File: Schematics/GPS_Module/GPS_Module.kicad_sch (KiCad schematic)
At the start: 70 parts, among them J1 GT8E-6P-2H(55), J2 SWD_01x04_Pin, J4 Stack Male Edge Connector, J4 USB_C_Female_USB2_Small, Q1 AO3400A, SW1 SW_STM_RESET, SW2 SW_STM_BOOT_MODE, U1 STM32F103CBT6, U12 AMS1117-3.3, U2 W25Q128JVS, U4 LM66100DCKR, U5 LM66100DCKR, U6 LM66100DCKR, U8 ACS70331EOLC, U9 ISO1042BQDWVR, Y1 X322516MMB4SI

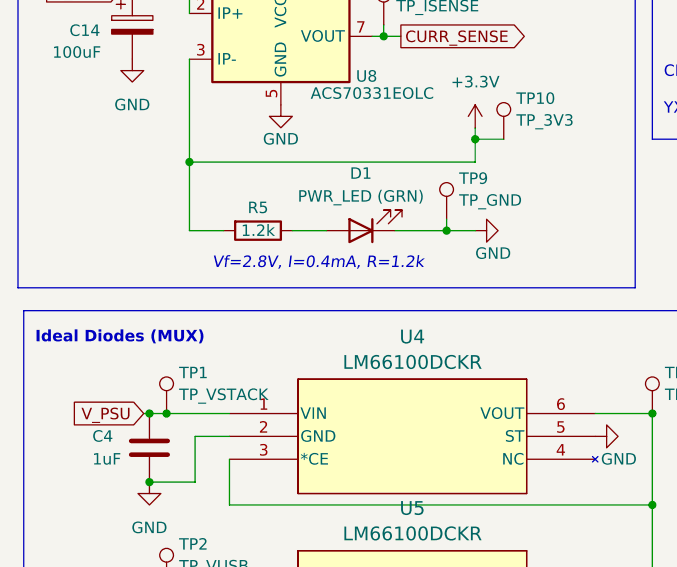
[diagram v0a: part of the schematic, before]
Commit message: Reduced PWR LED brightness (3.3k resistor)
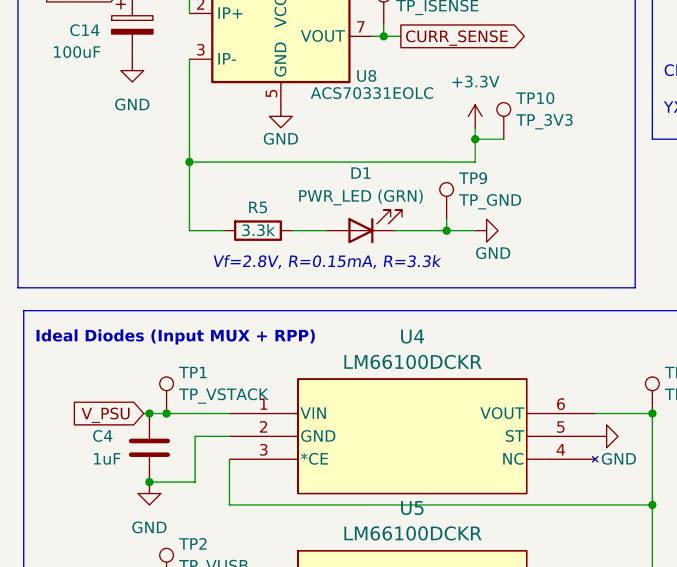
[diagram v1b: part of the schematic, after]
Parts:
- R5: value 1.2k -> 3.3k; LCSC C22765 -> C22978
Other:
- note added: "Ideal Diodes (Input MUX + RPP)"
- note added: "Vf=2.8V, R=0.15mA, R=3.3k"
- note removed: "Ideal Diodes (MUX)"
- note removed: "Vf=2.8V, I=0.4mA, R=1.2k"
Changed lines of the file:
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@@
     (effects (font (size 1.27 1.27)) (justify left bottom))
   )
-  (text "Ideal Diodes (MUX)" (at 15.875 74.93 0)
+  (text "Ideal Diodes (Input MUX + RPP)" (at 15.875 74.93 0)
     (effects (font (size 1.27 1.27) (thickness 0.254) bold) (justify left bottom))
   )
@@
     (effects (font (size 1.27 1.27) (thickness 0.254) bold) (justify left bottom))
   )
-  (text "Vf=2.8V, I=0.4mA, R=1.2k" (at 35.56 66.675 0)
+  (text "Vf=2.8V, R=0.15mA, R=3.3k" (at 35.56 66.675 0)
     (effects (font (size 1.27 1.27) italic) (justify left bottom))
   )
@@
       (effects (font (size 1.27 1.27)))
     )
-    (property "Value" "1.2k" (at 40.64 62.23 90)
+    (property "Value" "3.3k" (at 40.64 62.23 90)
       (effects (font (size 1.27 1.27)))
     )
@@
       (effects (font (size 1.27 1.27)) hide)
     )
-    (property "LCSC" "C22765" (at 40.64 62.23 0)
+    (property "LCSC" "C22978" (at 40.64 62.23 0)
       (effects (font (size 1.27 1.27)) hide)
     )

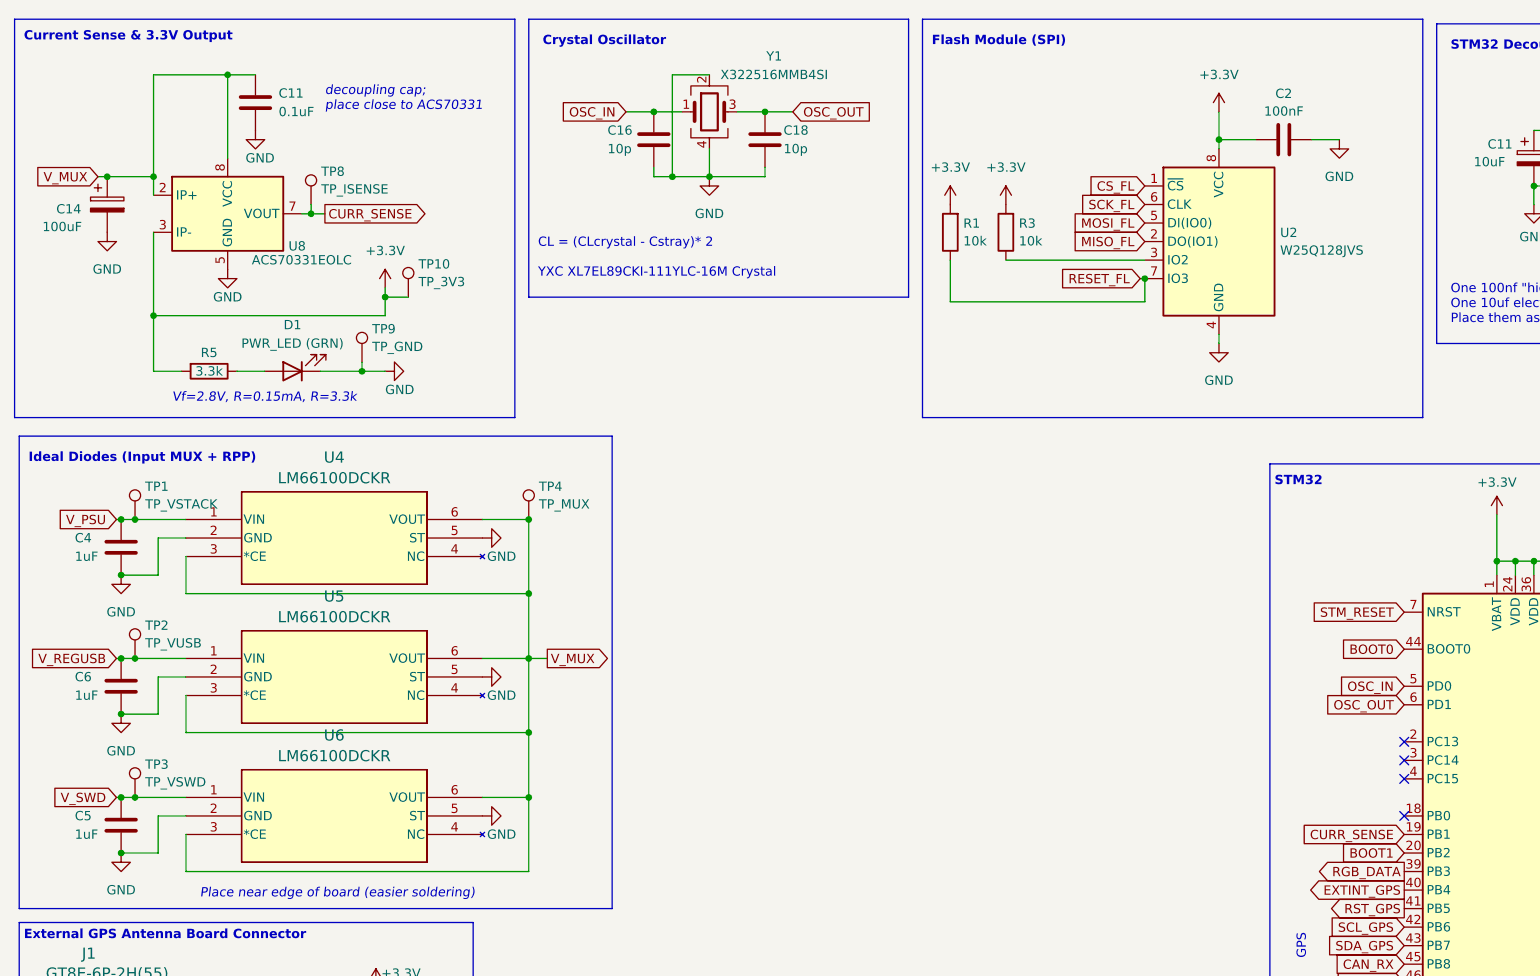
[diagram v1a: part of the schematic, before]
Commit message: Removed ACS70331 current sensor
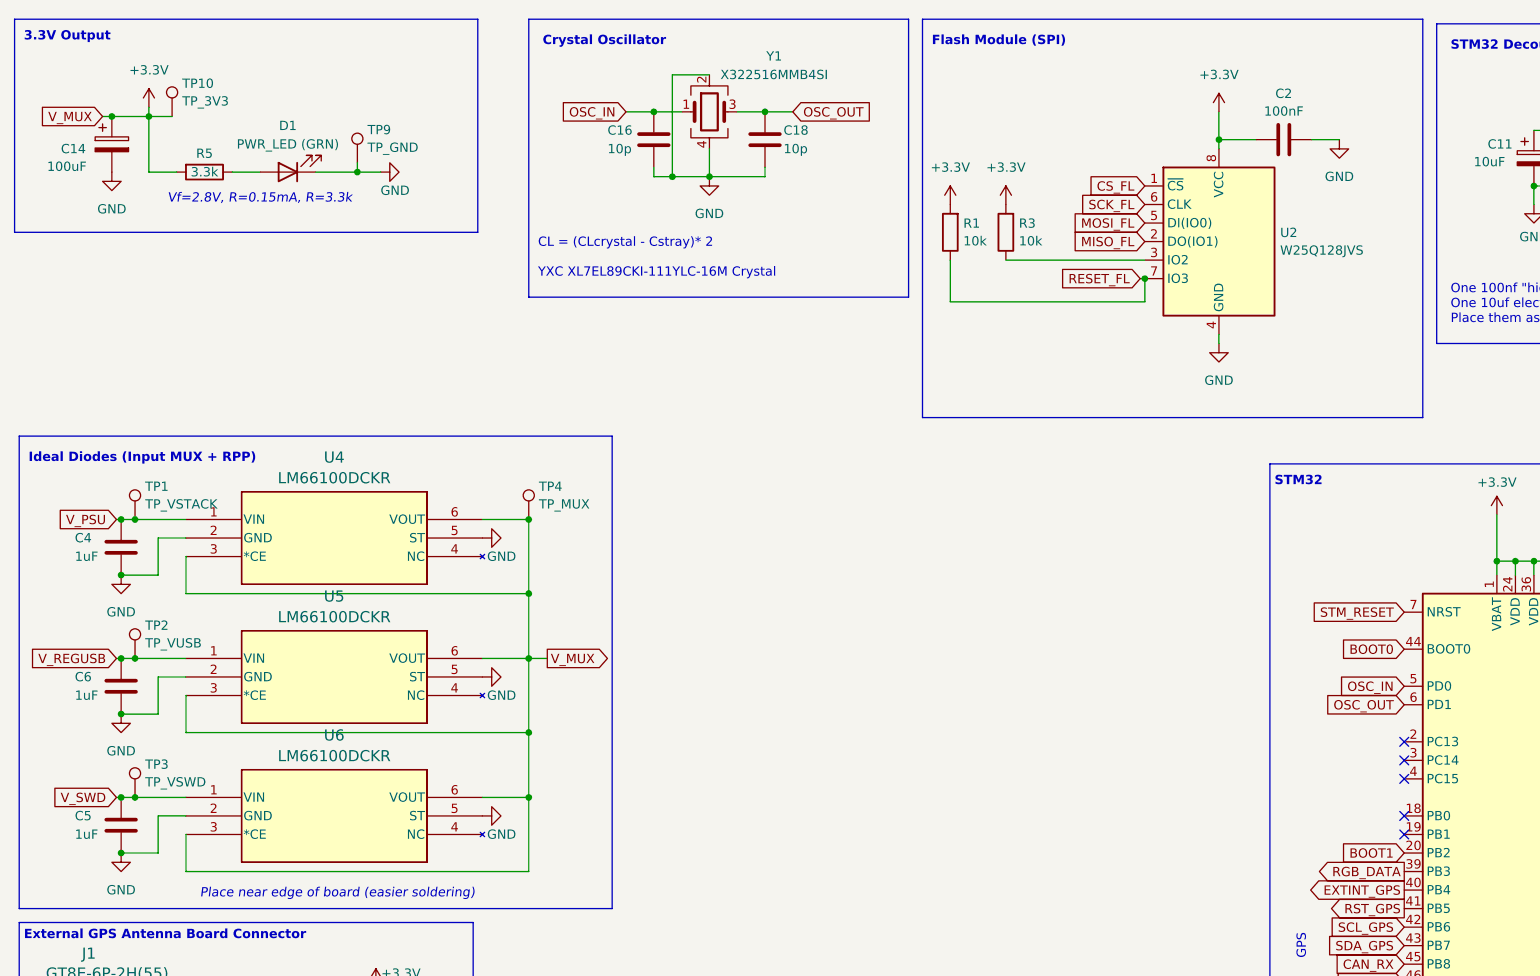
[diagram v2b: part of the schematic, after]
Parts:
- removed C11: 0.1uF, Capacitor_SMD:C_0603_1608Metric, symbol Device:C
- removed TP8: TP_ISENSE, TestPoint:TestPoint_Pad_1.5x1.5mm, symbol Connector:TestPoint
- removed U8: ACS70331EOLC, footprints:SOIC127P600X175-8N, symbol Sensor_Current:ACS706xLC-05C
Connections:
- net V_MUX is gone; now on net +3.3V: C14.1, TP4.1, U4.3 (*CE), U4.6 (VOUT), U5.3 (*CE), U5.6 (VOUT), U6.3 (*CE), U6.6 (VOUT)
- net CURR_SENSE: no longer names the net of U1.19 (PB1)
- no-connect marks 20 -> 21
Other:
- note added: "3.3V Output"
- note removed: "Current Sense & 3.3V Output"
- note removed: "decoupling cap; place close to ACS70331"
- moved on the sheet: C14, D1, R5, TP10, TP9

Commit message: Replaced "LCSC" fields with "JLCPCB" fields
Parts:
- C1, C3: JLCPCB (none) -> C96446; LCSC C96446 -> (none)
- C10, C12, C13, C9: JLCPCB (none) -> C1525; LCSC C1525 -> (none)
- C14: JLCPCB (none) -> C57112; LCSC C57112 -> (none)
- C16, C18: JLCPCB (none) -> C1634; LCSC C1634 -> (none)
- C2, C? (x3): JLCPCB (none) -> C14663; LCSC C14663 -> (none)
- C20, C21: JLCPCB (none) -> C28323; LCSC C28323 -> (none)
- C4, C5, C6: JLCPCB (none) -> C15849; LCSC C15849 -> (none)
- D1: JLCPCB (none) -> C2297; LCSC C2297 -> (none)
- D2, D3: JLCPCB (none) -> C191023; LCSC C191023 -> (none)
- D5: JLCPCB (none) -> C72038; LCSC C72038 -> (none)
- FB1: JLCPCB (none) -> C1015; LCSC C1015 -> (none)
- J4: JLCPCB (none) -> C2936184; LCSC C2936184 -> (none)
- Q1: JLCPCB (none) -> C20917; LCSC C20917 -> (none)
- R1, R10, R3: JLCPCB (none) -> C25804; LCSC C25804 -> (none)
- R11, R6: JLCPCB (none) -> C25803; LCSC C25803 -> (none)
- R11: JLCPCB (none) -> C23228; LCSC C23228 -> (none)
- R12: JLCPCB (none) -> C21190; LCSC C21190 -> (none)
- R28, R29: JLCPCB (none) -> C23186; LCSC C23186 -> (none)
- R5, R6: JLCPCB (none) -> C4190; LCSC C4190 -> (none)
- R5: JLCPCB (none) -> C22978; LCSC C22978 -> (none)
- R8: JLCPCB (none) -> C22843; LCSC C22843 -> (none)
- R9: JLCPCB (none) -> C23193; LCSC C23193 -> (none)
- SW1, SW2: JLCPCB (none) -> C318884; LCSC C318884 -> (none)
- U1: JLCPCB (none) -> C8304; LCSC C8304 -> (none)
- U12: JLCPCB (none) -> C6186; LCSC C6186 -> (none)
- U2: JLCPCB (none) -> C97521; LCSC C97521 -> (none)
- U4, U5, U6: JLCPCB (none) -> C2869734; LCSC C2869734 -> (none)
- U9: JLCPCB (none) -> C484409; LCSC C484409 -> (none)
- Y1: JLCPCB (none) -> C13738; LCSC C13738 -> (none)

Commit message: Changed SWD programming header to SMD version
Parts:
- J2: footprint SWD_Header:SWD_PinHeader_1x04_P2.54mm_Horizontal -> SWD_Header:SWD_PinHeader_1x04_P2.54mm_Horizontal_SMD; Digikey 2057-PH1RB-04-UA-ND -> 952-3233-ND
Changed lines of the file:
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@@
       (effects (font (size 1.27 1.27)) (justify right))
     )
-    (property "Footprint" "SWD_Header:SWD_PinHeader_1x04_P2.54mm_Horizontal" (at 388.62 160.655 0)
+    (property "Footprint" "SWD_Header:SWD_PinHeader_1x04_P2.54mm_Horizontal_SMD" (at 388.62 160.655 0)
       (effects (font (size 1.27 1.27)) hide)
     )
@@
       (effects (font (size 1.27 1.27)) hide)
     )
-    (property "Digikey" "2057-PH1RB-04-UA-ND" (at 388.62 170.18 0)
+    (property "Digikey" "952-3233-ND" (at 388.62 170.18 0)
       (effects (font (size 1.27 1.27)) hide)
     )

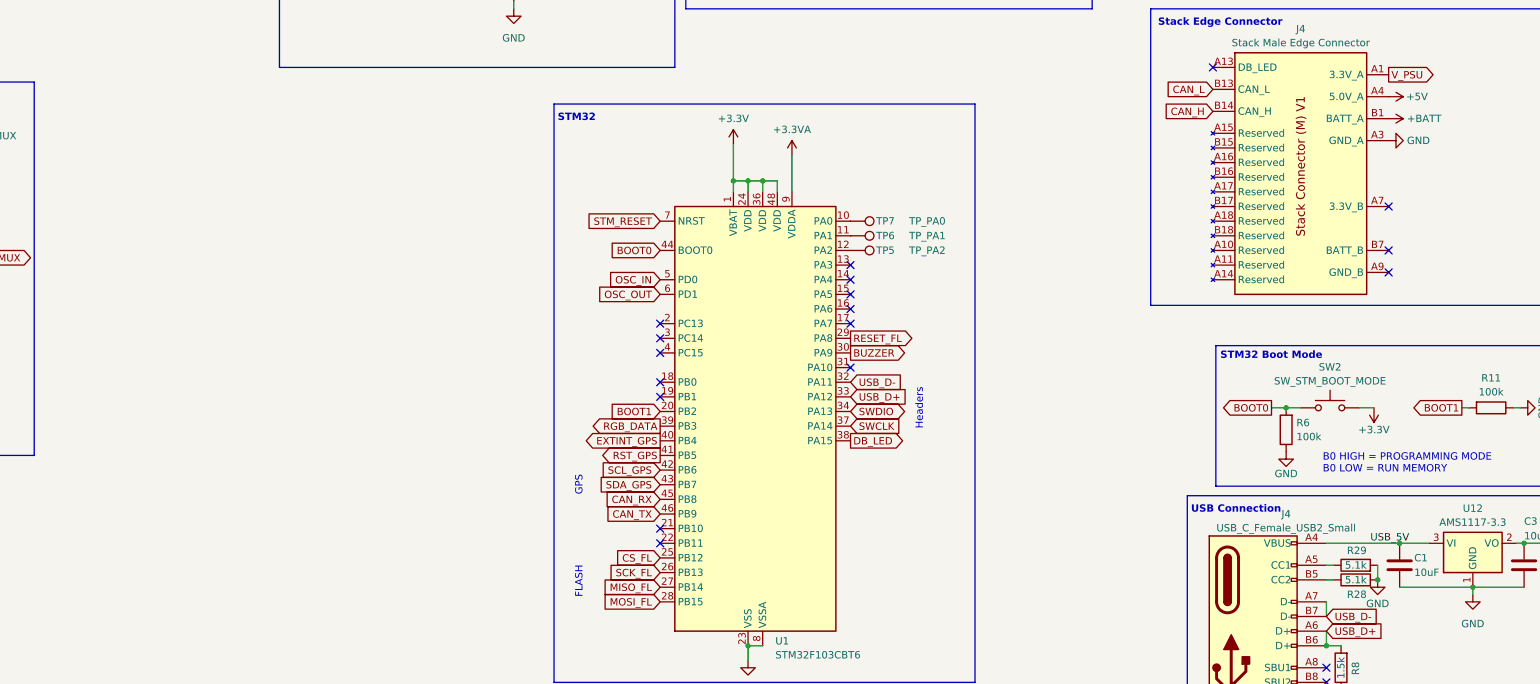
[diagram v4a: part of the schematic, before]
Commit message: Added CP2102 USB-UART bridge
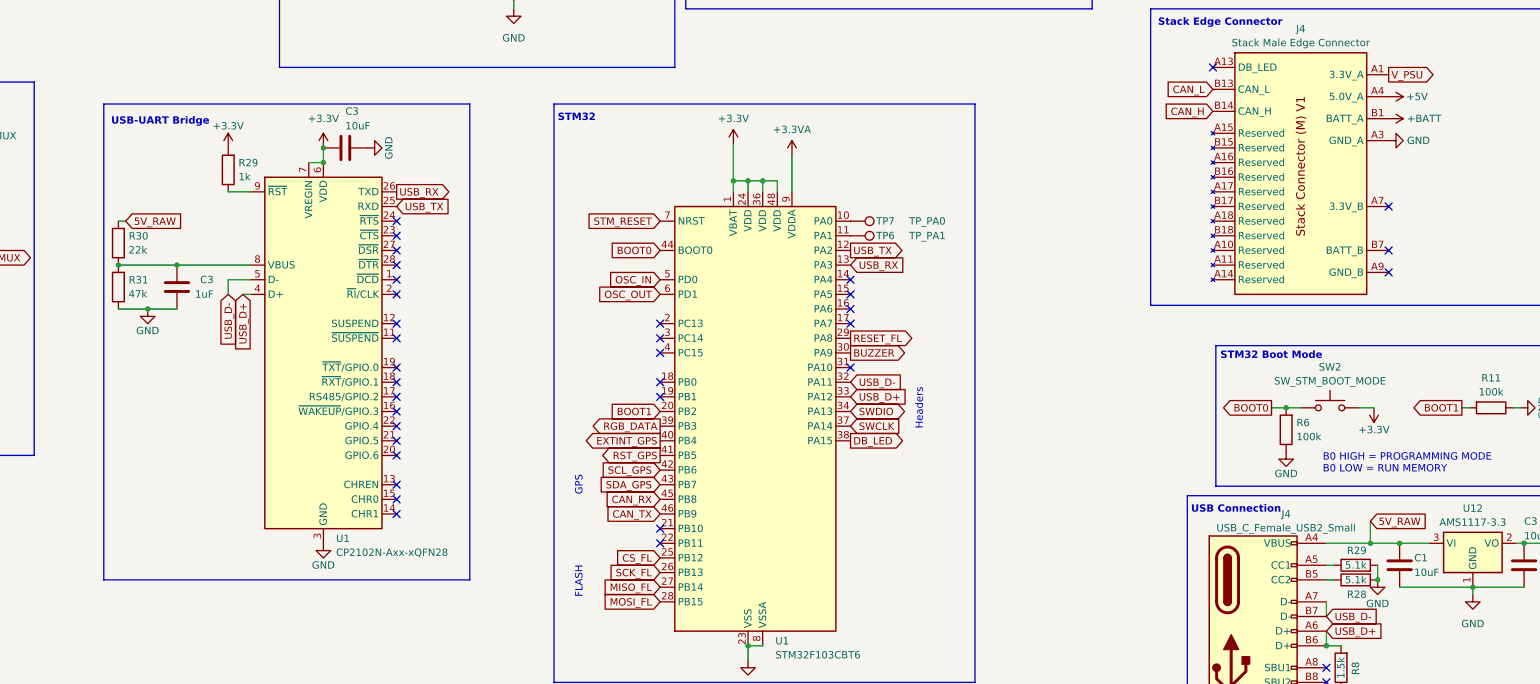
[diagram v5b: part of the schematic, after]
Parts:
- removed TP5: TP_PA2, TestPoint:TestPoint_Pad_1.5x1.5mm, symbol Connector:TestPoint
- added C3: 1uF, Capacitor_SMD:C_0603_1608Metric, symbol Device:C
- added C3: 10uF, Capacitor_SMD:C_0603_1608Metric, symbol Device:C
- added R29: 1k, Resistor_SMD:R_0603_1608Metric, symbol Device:R
- added R30: 22k, Resistor_SMD:R_0603_1608Metric, symbol Device:R
- added R31: 47k, Resistor_SMD:R_0603_1608Metric, symbol Device:R
- added U1: CP2102N-Axx-xQFN28, Package_DFN_QFN:QFN-28-1EP_5x5mm_P0.5mm_EP3.35x3.35mm, symbol Interface_USB:CP2102N-Axx-xQFN28
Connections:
- net +3.3V: now also C3.2, R29.2, U1.6 (VDD), U1.7 (VREGIN)
- net GND: now also C3.1, C3.1, R31.1, U1.29 (GND), U1.3 (GND)
- net USB_D+: now also U1.4 (D+)
- net USB_D-: now also U1.5 (D-)
- net USB_TX: now reaches U1.12 (PA2)
- net USB_TX: now also U1.25 (RXD)
- net USB_RX: now reaches U1.13 (PA3)
- net USB_RX: now also U1.26 (TXD)
- net USB_5V renamed 5V_RAW
- net 5V_RAW: now also R30.2
- new net: C3.2, R30.1, R31.2, U1.8 (VBUS)
- new net: R29.1, U1.9 (~{RST})
- no-connect marks 21 -> 38
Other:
- note added: "USB-UART Bridge"
